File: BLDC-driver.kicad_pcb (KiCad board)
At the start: 2 copper layers, 52.2 x 52.2 mm, 83 parts, among them J1 Conn_01x06, J2 Conn_01x06, Q1 FDMS86550, Q2 FDMS86550, Q3 FDMS86550, Q4 FDMS86550, Q5 FDMS86550, Q6 FDMS86550, U1 ADP3120A, U2 STM32F103C8Tx, U3 MAX3051, U4 ADP3120A, U5 ADP3120A, U6 MP2359, U7 MIC5504-3.3YM5, U8 NCS210, U9 NCS210

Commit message: Latest
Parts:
- removed C22: 2.7nF, Capacitor_SMD:C_0603_1608Metric
- removed R4, R5, R6: 2.2, Resistor_SMD:R_0603_1608Metric
- added Y1: 8MHz, Crystal:Resonator_SMD_muRata_CSTxExxV-3Pin_3.0x1.1mm, F.Cu at (177.5, 134.9)
- C1, C10, C11, C12, C15, C16, C17, C2, C27, C3: value 4.7uF -> 10uF
- C20, C21: value 2.7nF -> 100nF; footprint Capacitor_SMD:C_0603_1608Metric -> Capacitor_SMD:C_0402_1005Metric
- C23: value 10nF -> 100nF
- C24: value 1uF -> 4.7uF
- D4, D5, D6: value 45V -> 30V; footprint Diode_SMD:D_SOD-523 -> Diode_SMD:D_SOD-323
- Q1, Q2, Q3, Q4, Q5, Q6: value FDMS86550 -> FDMS8018
- R19, R20: value 10k -> 2.2k; footprint Resistor_SMD:R_0603_1608Metric -> Resistor_SMD:R_0402_1005Metric
- R21, R22: value 10k -> 2.2k
- R23, R24: value 10k -> 1k
- R8: value 47k -> 33k
- R9: value 9.1k -> 5.6k
- U1, U4, U5: value ADP3120A -> NCP81151B
- moved C21 30.1 mm to (178.8, 112.3), turned to 180 degrees
- moved C20 28.3 mm to (219.1, 126.3), turned to 90 degrees
- moved D4 1.55 mm to (201.5, 109.3), turned to 270 degrees
- moved D5 1.06 mm to (194.1, 110.0)
- moved R19 0.99 mm to (220.1, 126.3)
- moved R20 0.53 mm to (218.1, 126.3)
- moved C19 0.48 mm to (188.5, 112.1)
- moved D6 0.37 mm to (186.8, 109.7)
- moved R10 0.36 mm to (182.5, 134.6)
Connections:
- C20 pad 2: GNDPWR -> GND
- C21 pad 2: GNDPWR -> GND
- R19 pad 2: Net-(R19-Pad2) -> Net-(C20-Pad1)
- R20 pad 2: Net-(R19-Pad2) -> Net-(C20-Pad1)
- R21 pad 1: Net-(R21-Pad1) -> Net-(C21-Pad1)
- R22 pad 1: Net-(R21-Pad1) -> Net-(C21-Pad1)
- U8 pad 1: Net-(R19-Pad2) -> Net-(C20-Pad1)
- U9 pad 1: Net-(R21-Pad1) -> Net-(C21-Pad1)
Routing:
- net GNDPWR: track 102.9 -> 95.7 mm, vias 97 -> 96
- net Net-(C20-Pad1): track 1.46 -> 7.95 mm
- net Net-(U2-Pad6): track 0.00 -> 6.19 mm
- net Net-(R19-Pad2): track 5.56 -> 0.00 mm
- net Net-(U2-Pad5): track 0.00 -> 4.62 mm
- net Net-(R21-Pad1): track 4.14 -> 0.00 mm
- net Net-(C21-Pad1): track 1.51 -> 5.30 mm
- net GND: track 55.4 -> 53.6 mm
- net Net-(C13-Pad2): track 4.21 -> 5.84 mm
- net Net-(C22-Pad1): track 1.46 -> 0.00 mm
- net +3V3: track 148.7 -> 149.9 mm
- net Net-(C7-Pad2): track 3.01 -> 4.01 mm
- net /SDA: track 28.6 -> 28.0 mm
- net +24V: vias 70 -> 66

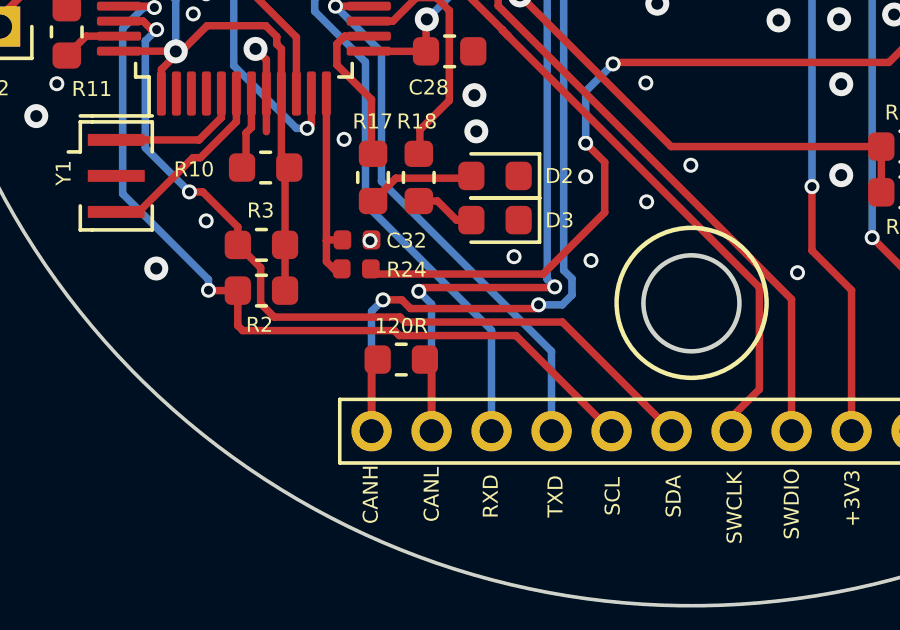
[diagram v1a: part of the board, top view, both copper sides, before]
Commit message: Change i2c resistor to 2.2k
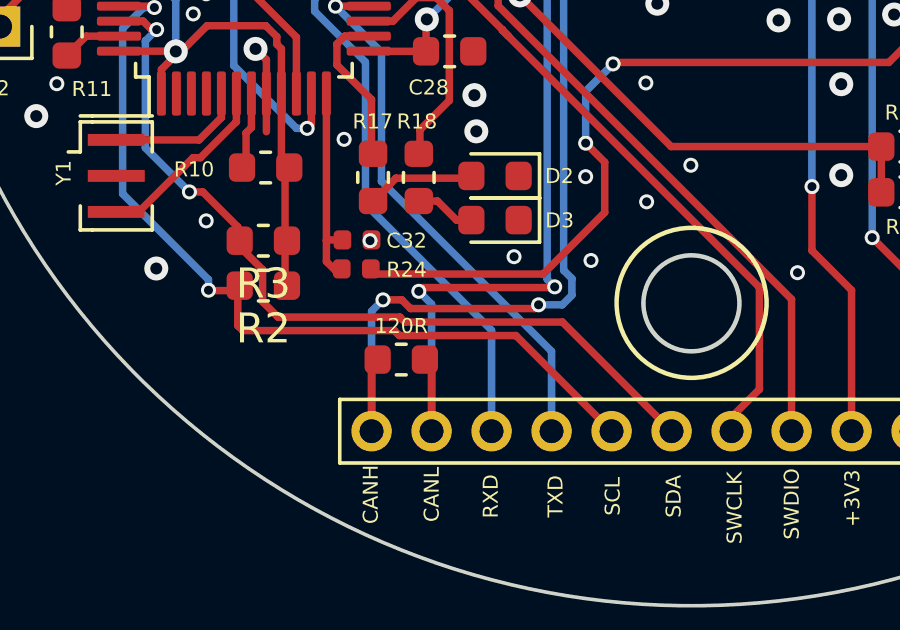
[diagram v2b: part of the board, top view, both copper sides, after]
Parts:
- R2, R3: value 10k -> 2.2k
- moved R2 0.18 mm to (182.4, 138.6)
- moved R3 0.15 mm to (182.4, 137.1)

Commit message: add pwm 5v pull up
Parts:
- added R4: 1k, Resistor_SMD:R_0402_1005Metric, F.Cu at (194.1, 112.3)
- added R5: 1k, Resistor_SMD:R_0402_1005Metric, F.Cu at (203.4, 108.7)
- added R6: 1k, Resistor_SMD:R_0402_1005Metric, F.Cu at (184.7, 111.5)
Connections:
- U2 pad 18: Net-(U2-Pad18) -> (no net)
- U2 pad 19: Net-(U2-Pad19) -> (no net)
- U2 pad 2: Net-(U2-Pad2) -> (no net)
- U2 pad 20: Net-(U2-Pad20) -> (no net)
- U2 pad 21: Net-(U2-Pad21) -> (no net)
- U2 pad 22: Net-(U2-Pad22) -> (no net)
- U2 pad 25: Net-(U2-Pad25) -> (no net)
- U2 pad 26: Net-(U2-Pad26) -> (no net)
- U2 pad 27: Net-(U2-Pad27) -> (no net)
- U2 pad 28: Net-(U2-Pad28) -> (no net)
- U2 pad 3: Net-(U2-Pad3) -> (no net)
- U2 pad 4: Net-(U2-Pad4) -> (no net)
- U7 pad 4: Net-(U7-Pad4) -> (no net)
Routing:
- net +5V: track 123.3 -> 125.5 mm
- net /PWM_B: track 74.1 -> 74.8 mm

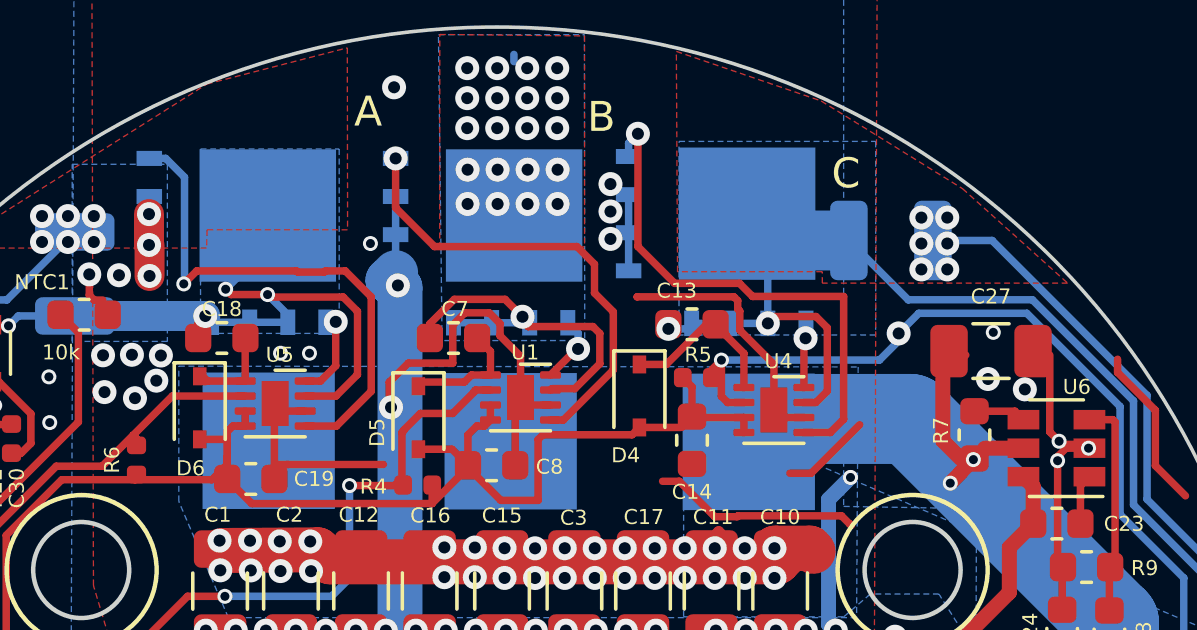
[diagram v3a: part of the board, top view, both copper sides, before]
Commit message: Add snubbers
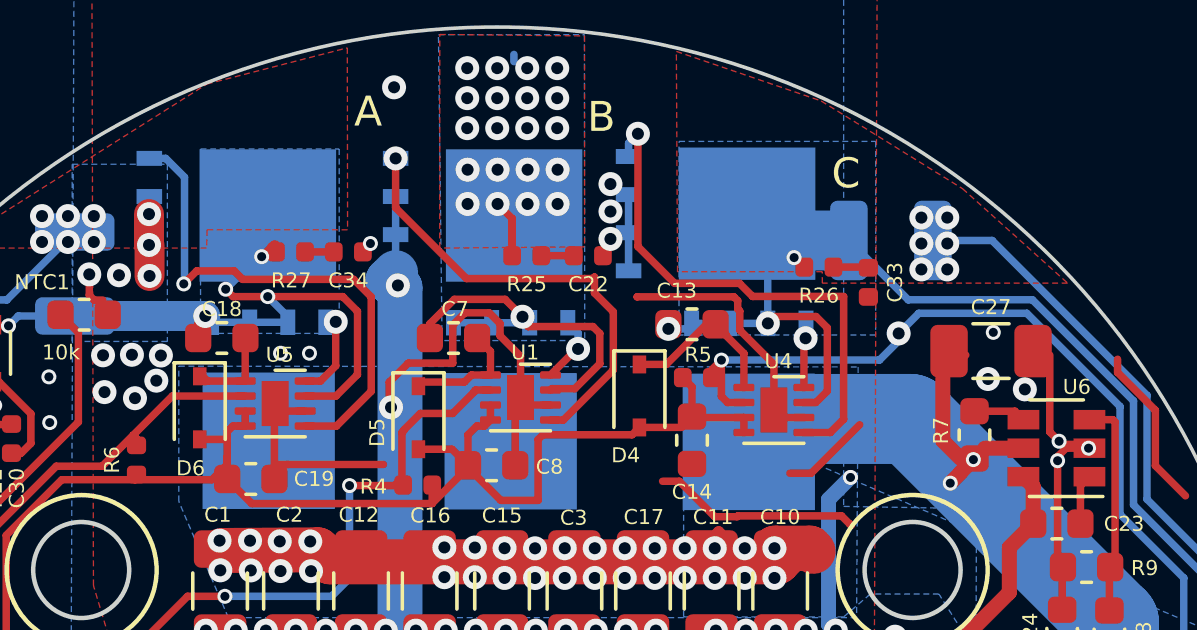
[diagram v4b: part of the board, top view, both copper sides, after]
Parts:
- added C22: 2.7nF, Capacitor_SMD:C_0402_1005Metric, F.Cu at (199.8, 104.6)
- added C33: 2.7nF, Capacitor_SMD:C_0402_1005Metric, F.Cu at (209.1, 105.5)
- added C34: 2.7nF, Capacitor_SMD:C_0402_1005Metric, F.Cu at (191.8, 104.5)
- added R25: 2.2R, Resistor_SMD:R_0402_1005Metric, F.Cu at (197.7, 104.6)
- added R26: 2.2R, Resistor_SMD:R_0402_1005Metric, F.Cu at (207.5, 105.0)
- added R27: 2.2R, Resistor_SMD:R_0402_1005Metric, F.Cu at (189.8, 104.5)
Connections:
- U2 pad 18: (no net) -> Net-(U2-Pad18)
- U2 pad 19: (no net) -> Net-(U2-Pad19)
- U2 pad 2: (no net) -> Net-(U2-Pad2)
- U2 pad 20: (no net) -> Net-(U2-Pad20)
- U2 pad 21: (no net) -> Net-(U2-Pad21)
- U2 pad 22: (no net) -> Net-(U2-Pad22)
- U2 pad 25: (no net) -> Net-(U2-Pad25)
- U2 pad 26: (no net) -> Net-(U2-Pad26)
- U2 pad 27: (no net) -> Net-(U2-Pad27)
- U2 pad 28: (no net) -> Net-(U2-Pad28)
- U2 pad 3: (no net) -> Net-(U2-Pad3)
- U2 pad 4: (no net) -> Net-(U2-Pad4)
- U7 pad 4: (no net) -> Net-(U7-Pad4)
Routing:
- net /PH_A: track 13.3 -> 16.1 mm
- net Net-(C33-Pad1): track 0.00 -> 1.18 mm
- net Net-(C22-Pad1): track 0.00 -> 1.09 mm
- net Net-(C34-Pad1): track 0.00 -> 0.96 mm
- net /PH_C: track 24.2 -> 24.8 mm, vias 4 -> 5
- net /PH_B: track 42.2 -> 42.7 mm, vias 3 -> 4

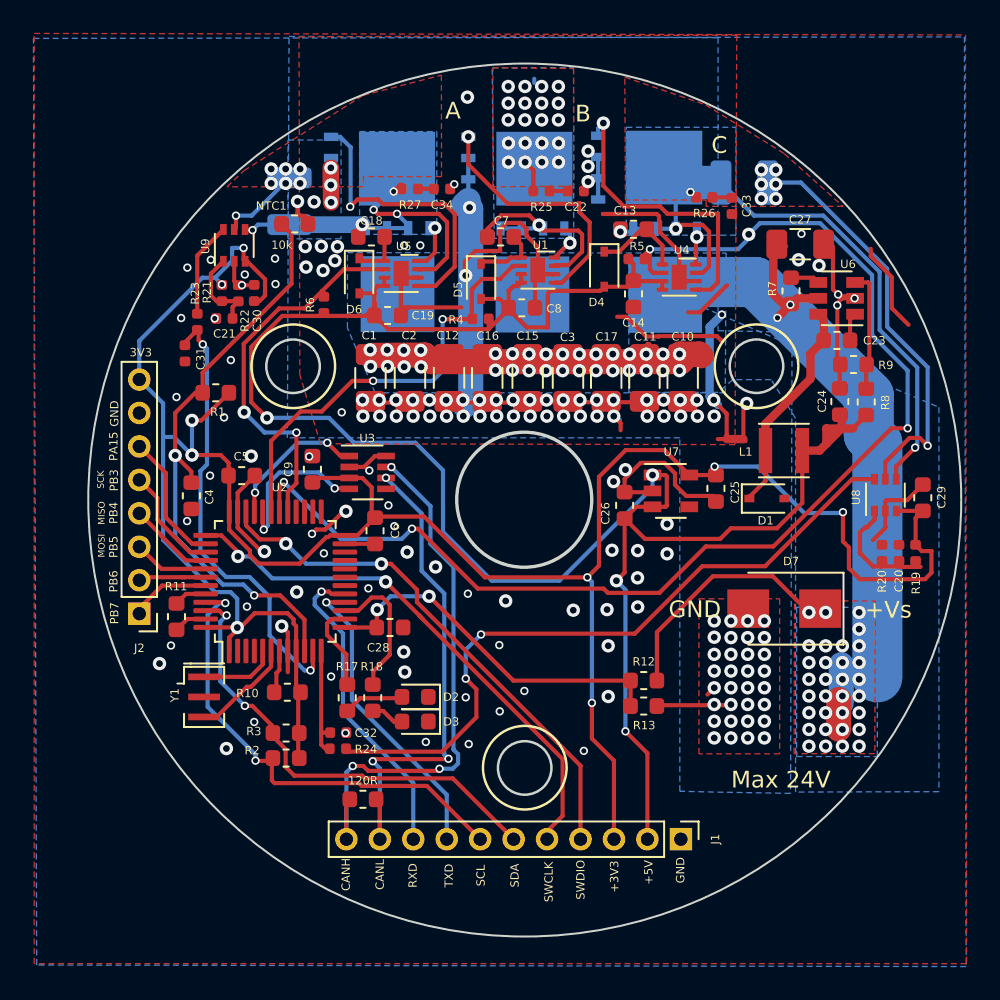
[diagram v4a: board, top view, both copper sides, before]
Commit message: Revision 2 update
Move current shunts to low side. I have encountered smoke from current
amplifiers when working @ 20V.
Adapt to STM32L4xxCBT mcu.
Add snubbers and resistance to gate drivers to reduce ringing due to
very fast switching.
Add RS485 interface instead of CAN
Route ENABLE signal to gate drivers
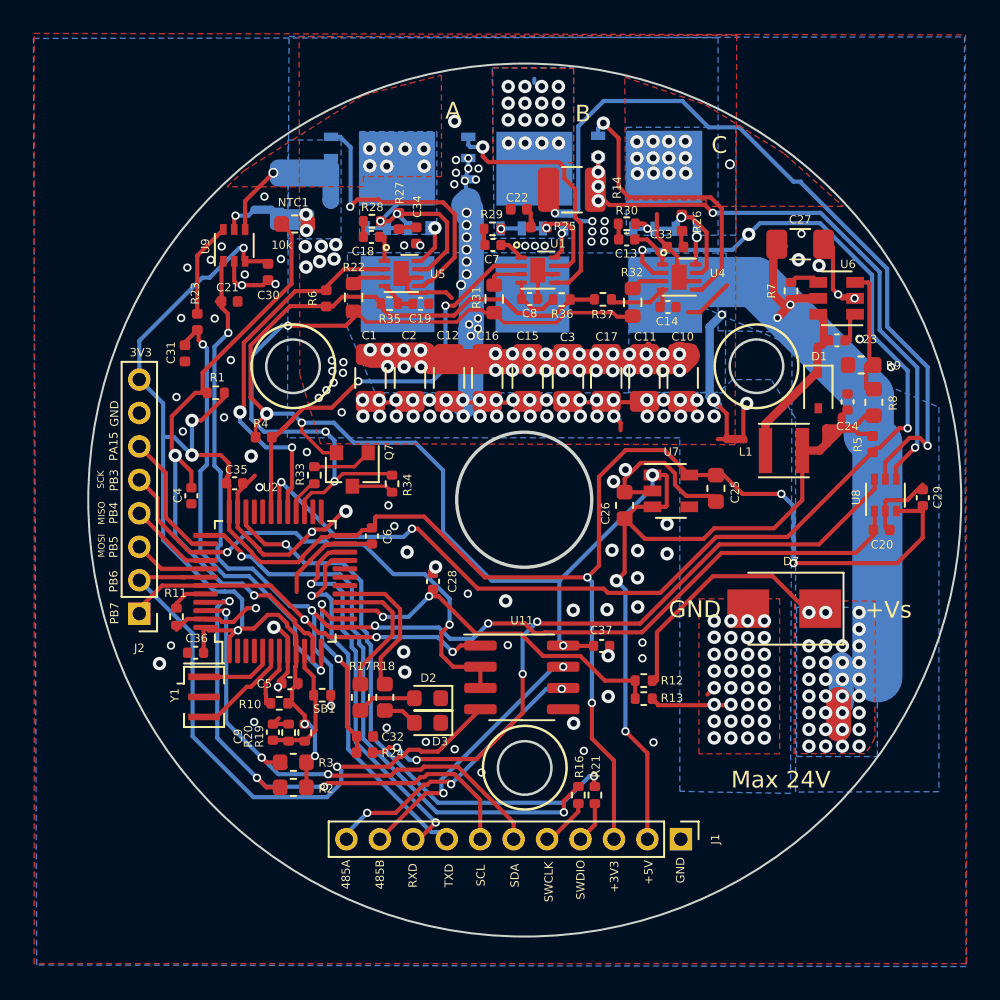
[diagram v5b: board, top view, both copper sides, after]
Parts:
- removed D4, D5, D6: 30V, Diode_SMD:D_SOD-323
- removed U3: MAX3051, Package_TO_SOT_SMD:SOT-23-8
- added C35: 100nF, Capacitor_SMD:C_0402_1005Metric, F.Cu at (179.4, 122.1)
- added C36: 100nF, Capacitor_SMD:C_0402_1005Metric, F.Cu at (177.0, 132.3)
- added C37: 100nF, Capacitor_SMD:C_0402_1005Metric, F.Cu at (201.3, 131.9)
- added NT2: Net-Tie_2, NetTie:NetTie-2_SMD_Pad0.5mm, B.Cu at (181.1, 105.8)
- added NT3: Net-Tie_2, NetTie:NetTie-2_SMD_Pad0.5mm, B.Cu at (199.0, 106.0)
- added Q7: BC807, Package_TO_SOT_SMD:SOT-23, F.Cu at (186.4, 121.3)
- added R28: 10, Resistor_SMD:R_0402_1005Metric, F.Cu at (187.6, 106.5)
- added R29: 10, Resistor_SMD:R_0402_1005Metric, F.Cu at (194.8, 106.9)
- added R30: 10, Resistor_SMD:R_0402_1005Metric, F.Cu at (202.8, 106.6)
- added R31: 0, Resistor_SMD:R_0603_1608Metric, F.Cu at (194.9, 111.1)
- added R32: 0, Resistor_SMD:R_0603_1608Metric, F.Cu at (203.2, 111.3)
- added R33: 1k, Resistor_SMD:R_0402_1005Metric, F.Cu at (184.1, 121.6)
- added R34: 1k, Resistor_SMD:R_0402_1005Metric, F.Cu at (188.8, 122.1)
- added R35: 1, Resistor_SMD:R_0402_1005Metric, F.Cu at (188.6, 111.4)
- added R36: 1, Resistor_SMD:R_0402_1005Metric, F.Cu at (198.9, 111.1)
- added R37: 1, Resistor_SMD:R_0402_1005Metric, F.Cu at (201.4, 111.1)
- added REF**: OSHW-Logo2_7.3x6mm_SilkScreen, Symbol:OSHW-Logo2_7.3x6mm_SilkScreen, B.Cu at (187.6, 131.7)
- added SB1: 0, Resistor_SMD:R_0402_1005Metric, F.Cu at (184.6, 134.8)
- added U11: SN75176AD, Package_SO:SOIC-8_3.9x4.9mm_P1.27mm, F.Cu at (196.5, 133.7)
- C13, C18, C23, C28, C29, C4, C5, C6, C7, C9: footprint Capacitor_SMD:C_0603_1608Metric -> Capacitor_SMD:C_0402_1005Metric
- C14, C19, C24, C8: value 4.7uF -> 1uF; footprint Capacitor_SMD:C_0603_1608Metric -> Capacitor_SMD:C_0402_1005Metric
- C22, C33, C34: value 2.7nF -> 22nF
- C31, C32: value 100nF -> 4.7nF
- R1, R10, R11, R12, R13, R7: footprint Resistor_SMD:R_0603_1608Metric -> Resistor_SMD:R_0402_1005Metric
- R14: moved to F.Cu
- R16: value 120R -> 100; footprint Resistor_SMD:R_0603_1608Metric -> Resistor_SMD:R_0402_1005Metric
- R19, R20: value 2.2k -> 1k
- R21: value 2.2k -> 100
- R22: value 2.2k -> 0; footprint Resistor_SMD:R_0402_1005Metric -> Resistor_SMD:R_0603_1608Metric
- R23, R24: value 1k -> 100
- R25, R26, R27: value 2.2R -> 1R
- R9: value 5.6k -> 6.2k
- U2: value STM32F103C8Tx -> STM32L412CB
- moved R19 38.1 mm to (183.6, 137.0)
- moved R21 37.4 mm to (200.9, 140.8), turned to 270 degrees
- moved R20 37.1 mm to (182.6, 137.0), turned to 90 degrees
- moved R5 17.9 mm to (217.5, 119.8), turned to 90 degrees
- moved C9 15.9 mm to (181.7, 137.0), turned to 270 degrees
- moved R4 14.8 mm to (181.1, 119.4), turned to 180 degrees
- moved R16 12.9 mm to (199.9, 140.8), turned to 270 degrees
- moved C5 12.8 mm to (182.7, 134.1), turned to 0 degrees
- moved R14 10.3 mm to (199.5, 104.6), turned to 0 degrees
- moved D1 7.15 mm to (214.3, 116.6), turned to 270 degrees
- moved R22 6.90 mm to (186.5, 111.0)
- moved C33 4.18 mm to (205.7, 108.0), turned to 180 degrees
- moved C28 3.77 mm to (191.2, 128.0), turned to 270 degrees
- moved C22 3.57 mm to (196.4, 105.7), turned to 180 degrees
- moved C34 3.18 mm to (190.2, 107.3), turned to 270 degrees
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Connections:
- net /PB3 renamed /U1_DE
- net /PB6 renamed /U1_TX
- net /PB7 renamed /U1_RX
- C13 pad 1: /PH_B -> Net-(C13-Pad1)
- C14 pad 1: +5V -> Net-(C14-Pad1)
- C18 pad 1: /PH_C -> Net-(C18-Pad1)
- C19 pad 1: +5V -> Net-(C19-Pad1)
- C20 pad 1: Net-(C20-Pad1) -> /VREF_OUT
- C21 pad 1: Net-(C21-Pad1) -> /VREF_OUT
- C7 pad 1: /PH_A -> Net-(C7-Pad1)
- C8 pad 1: +5V -> Net-(C8-Pad1)
- C9 pad 1: +3V3 -> GND
- C9 pad 2: GND -> Net-(C9-Pad2)
- J1 pad 10: /CANL -> /485B
- J1 pad 11: /CANH -> /485A
- J1 pad 4: /SWDIO -> Net-(J1-Pad4)
- J1 pad 5: /SWCLK -> Net-(J1-Pad5)
- Q4 pad 1: GNDPWR -> /PHB_SH
- Q4 pad 2: GNDPWR -> /PHB_SH
- Q4 pad 3: GNDPWR -> /PHB_SH
- Q6 pad 1: GNDPWR -> /PHC_SH
- Q6 pad 2: GNDPWR -> /PHC_SH
- Q6 pad 3: GNDPWR -> /PHC_SH
- R14 pad 1: /PHB_SH -> GNDPWR
- R14 pad 2: /PH_B -> /PHB_SH
- R15 pad 1: /PHC_SH -> GNDPWR
- R15 pad 2: /PH_C -> /PHC_SH
- R16 pad 1: /CANH -> /SWCLK
- R16 pad 2: /CANL -> Net-(J1-Pad5)
- R19 pad 2: Net-(C20-Pad1) -> Net-(C9-Pad2)
- R20 pad 1: GND -> Net-(C9-Pad2)
- R20 pad 2: Net-(C20-Pad1) -> GND
- R21 pad 1: Net-(C21-Pad1) -> /SWDIO
- R21 pad 2: +3V3 -> Net-(J1-Pad4)
- R22 pad 1: Net-(C21-Pad1) -> /ENBL
- R22 pad 2: GND -> Net-(R22-Pad2)
- U1 pad 3: +5V -> Net-(R31-Pad2)
- U1 pad 4: +5V -> Net-(C8-Pad1)
- U2 pad 10: /FET_TEMP -> Net-(C9-Pad2)
- U2 pad 11: /CURR_C_FLT -> /FET_TEMP
- U2 pad 12: /CURR_B_FLT -> /CURR_C_FLT
- U2 pad 13: /VBUS -> /VREF_OUT
- U2 pad 14: /LEDR -> /CURR_B_FLT
- U2 pad 15: /LEDG -> /VBUS
- U2 pad 16: /TXD -> /LEDR
- U2 pad 17: /RXD -> /LEDG
- U2 pad 18: Net-(U2-Pad18) -> (no net)
- U2 pad 19: Net-(U2-Pad19) -> (no net)
- U2 pad 2: Net-(U2-Pad2) -> (no net)
- U2 pad 20: Net-(U2-Pad20) -> (no net)
- U2 pad 21: Net-(U2-Pad21) -> /TXD
- U2 pad 22: Net-(U2-Pad22) -> /RXD
- U2 pad 25: Net-(U2-Pad25) -> (no net)
- U2 pad 26: Net-(U2-Pad26) -> (no net)
- U2 pad 27: Net-(U2-Pad27) -> /ENBL
- U2 pad 3: Net-(U2-Pad3) -> (no net)
- U2 pad 32: /CANRX -> (no net)
- U2 pad 33: /CANTX -> (no net)
- U2 pad 4: Net-(U2-Pad4) -> (no net)
- U4 pad 3: +5V -> Net-(R32-Pad2)
- U4 pad 4: +5V -> Net-(C14-Pad1)
- U5 pad 3: +5V -> Net-(R22-Pad2)
- U5 pad 4: +5V -> Net-(C19-Pad1)
- U7 pad 4: Net-(U7-Pad4) -> (no net)
- U8 pad 1: Net-(C20-Pad1) -> /VREF_OUT
- U8 pad 4: /PH_B -> /PHB_SH
- U8 pad 5: /PHB_SH -> /PHB_GND
- U9 pad 1: Net-(C21-Pad1) -> /VREF_OUT
- U9 pad 4: /PH_C -> /PHC_SH
- U9 pad 5: /PHC_SH -> /PHC_GND
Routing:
- net /VREF_OUT: track 0.00 -> 71.6 mm, vias 0 -> 5
- net /PHB_GND: track 0.00 -> 44.7 mm, vias 0 -> 1
- net /ENBL: track 0.00 -> 43.3 mm, vias 0 -> 3
- net /CANH: track 33.3 -> 0.00 mm, vias 3 -> 0
- net /U1_TX: track 4.24 -> 36.8 mm, vias 0 -> 1
- net /CANL: track 30.3 -> 0.00 mm, vias 3 -> 0
- net /PH_B: track 42.7 -> 12.4 mm, vias 4 -> 15
- net GNDPWR: track 95.7 -> 69.6 mm, vias 96 -> 123
- net /U1_DE: track 6.51 -> 30.2 mm, vias 0 -> 2
- net /U1_RX: track 4.85 -> 22.6 mm, vias 0 -> 3
- net /485A: track 0.00 -> 17.0 mm, vias 0 -> 3
- net /485B: track 0.00 -> 15.9 mm, vias 0 -> 2
- net /PHB_SH: track 25.2 -> 36.7 mm, vias 7 -> 6
- net /PHC_SH: track 6.59 -> 16.5 mm, vias 7 -> 1
- net /CANRX: track 9.47 -> 0.00 mm, vias 2 -> 0
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- added copper zone on F.Cu, net /PH_B
- added copper zone on F.Cu, net /PH_C
- removed copper zone on F.Cu, net /PHB_SH
- removed copper zone on F.Cu, net /PHC_SH
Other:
- net class Default: clearance 0.2 -> 0.16
- rule pad_to_mask_clearance: 0.05 -> 0
- rule trace_clearance: 0.2 -> 0.16
- board text added: "485A"
- board text added: "485B"
- board text added: "FOC Drive Walmis@2021 REV2 www.ensys.lt"
- board text removed: "CANH"
- board text removed: "CANL"

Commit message: Multiple updates:
Change amp filter caps to 1nF
Move second shunt resistor to top layer
Make one hole grounded
various routing updates
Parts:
- added H1: MountingHole_Pad, MountingHole:MountingHole_3.2mm_M3_DIN965_Pad, F.Cu at (182.9, 115.1)
- C31, C32: value 4.7nF -> 1nF
- D7: value D_TVS -> SMAJ24A
- NT2, R15: moved to F.Cu
- U8, U9: value NCS210 -> NCS213RSQT2G
- moved NTC1 1.70 mm to (183.3, 108.3)
- moved R15 1.59 mm to (184.4, 105.3)
- moved NT2 1.48 mm to (181.7, 107.1)
- moved R6 0.37 mm to (185.2, 111.1)
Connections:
- U2 pad 18: (no net) -> Net-(U2-Pad18)
- U2 pad 19: (no net) -> Net-(U2-Pad19)
- U2 pad 2: (no net) -> Net-(U2-Pad2)
- U2 pad 20: (no net) -> Net-(U2-Pad20)
- U2 pad 25: (no net) -> Net-(U2-Pad25)
- U2 pad 26: (no net) -> Net-(U2-Pad26)
- U2 pad 3: (no net) -> Net-(U2-Pad3)
- U2 pad 32: (no net) -> /CANRX
- U2 pad 33: (no net) -> /CANTX
- U2 pad 4: (no net) -> Net-(U2-Pad4)
- U7 pad 4: (no net) -> Net-(U7-Pad4)
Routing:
- net /PHC_SH: track 16.5 -> 20.6 mm, vias 1 -> 6
- net /FET_TEMP: track 36.7 -> 34.8 mm
- net +5V: track 121.1 -> 119.3 mm
- net /ENBL: track 43.3 -> 44.8 mm
- net GNDPWR: track 69.6 -> 70.2 mm, vias 123 -> 127
- net /PWM_C: track 22.9 -> 23.5 mm
- net /PHC_GND: track 2.13 -> 2.65 mm, vias 1 -> 0
- net GND: vias 63 -> 62
- net /PH_C: vias 9 -> 10
- net /PH_B: vias 15 -> 14
- added copper zone on F.Cu, net /PHC_SH
